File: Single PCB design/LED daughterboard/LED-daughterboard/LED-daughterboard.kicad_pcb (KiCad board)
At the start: 2 copper layers, 23.4 x 17 mm, 9 parts, among them J1 Conn_01x03_Male, J2 Conn_01x02_Male

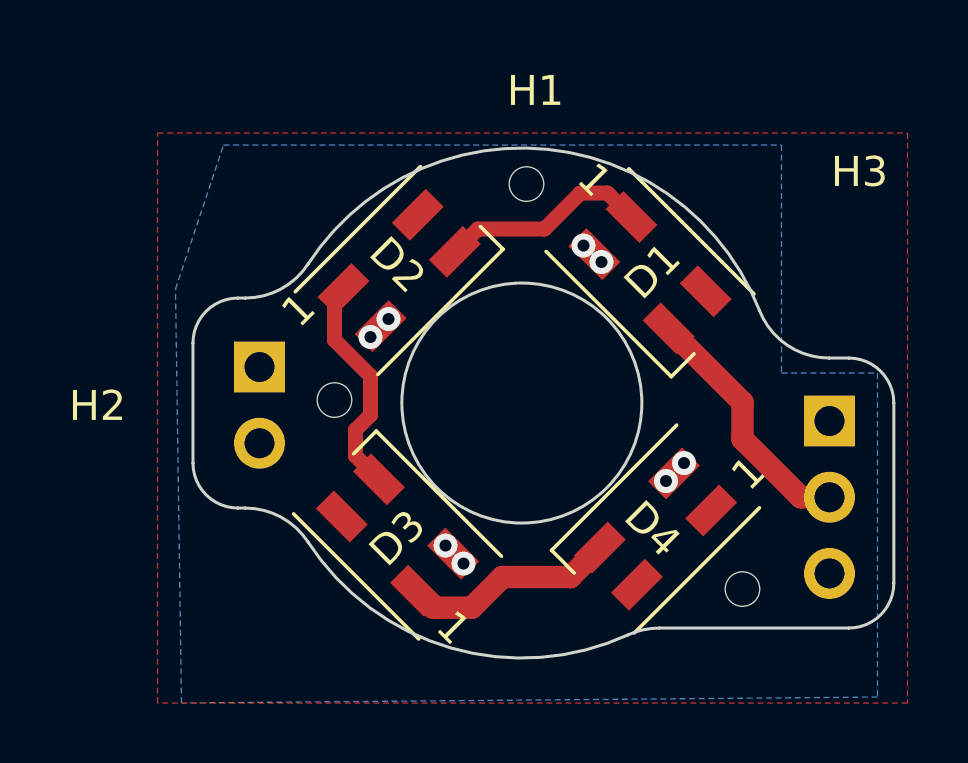
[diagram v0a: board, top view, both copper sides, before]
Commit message: Silkscreen changes
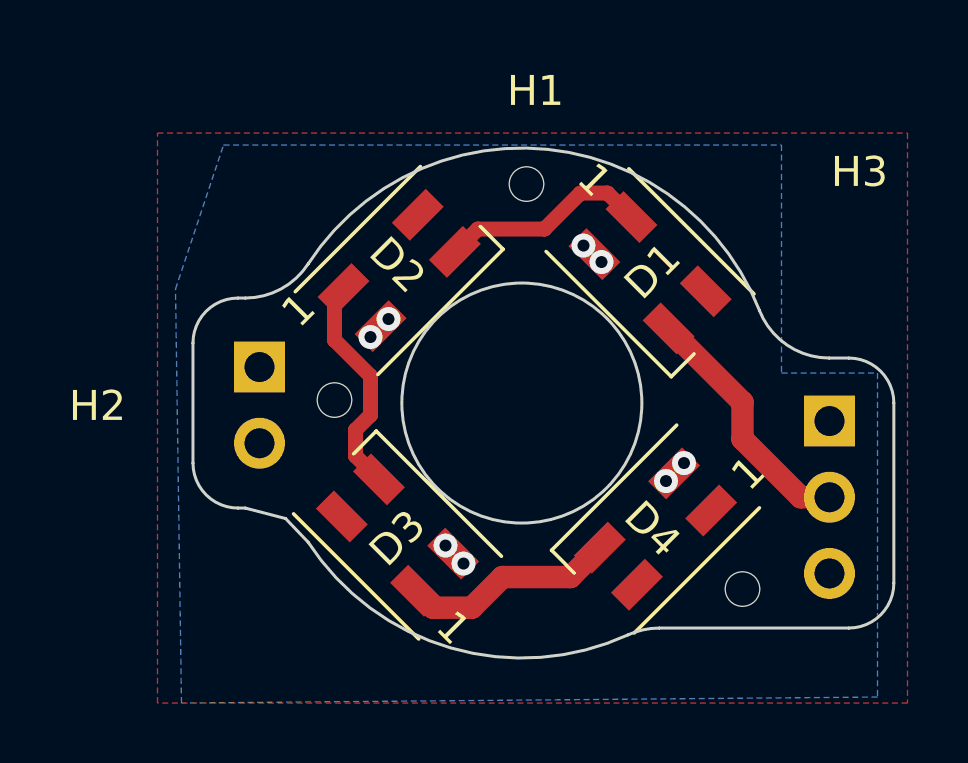
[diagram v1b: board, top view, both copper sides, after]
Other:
- outline, holes or cut-outs redrawn
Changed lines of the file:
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@@
   (general
     (thickness 1.6)
-    (drawings 17)
+    (drawings 18)
     (tracks 32)
     (modules 9)
@@
     )
   )
+  (gr_line (start -3.979118 -5.363636) (end -4.729925 -6.149999) (layer "Edge.Cuts") (width 0.1))
   (gr_arc (start -6.317425 -7.999999) (end -6.317425 -6.499999) (angle 90) (layer "Edge.Cuts") (width 0.1))
+  (gr_line (start 15.545075 -9.999999) (end 15.545075 -3.999999) (layer "Edge.Cuts") (width 0.1))
   (gr_arc (start 7.72765 0) (end 6.686156 -2.272727) (angle 24.61997733) (layer "Edge.Cuts") (width 0.1))
-  (gr_line (start 14.045075 -11.499999) (end 13.392025 -11.499999) (layer "Edge.Cuts") (width 0.1))
   (gr_arc (start -6.317425 -11.999999) (end -7.817425 -11.999999) (angle 90) (layer "Edge.Cuts") (width 0.1))
   (gr_line (start -7.817425 -11.999999) (end -7.817425 -7.999999) (layer "Edge.Cuts") (width 0.1))
@@
   (gr_arc (start 3.145075 -9.999999) (end -3.979119 -14.636363) (angle 125.6205826) (layer "Edge.Cuts") (width 0.1))
   (gr_arc (start 3.145075 -9.999999) (end 6.686156 -2.272727) (angle 81.56424618) (layer "Edge.Cuts") (width 0.1))
-  (gr_arc (start 13.392025 -13.999999) (end 13.392025 -11.499999) (angle 68.67631374) (layer "Edge.Cuts") (width 0.1))
+  (gr_arc (start 13.392026 -13.999999) (end 13.392026 -11.499999) (angle 68.67631374) (layer "Edge.Cuts") (width 0.1))
+  (gr_line (start -4.729925 -6.149999) (end -6.07447 -6.499999) (layer "Edge.Cuts") (width 0.1))
   (gr_circle (center 3.145075 -9.999999) (end -0.854925 -9.999999) (layer "Edge.Cuts") (width 0.1))
   (gr_line (start -6.317425 -6.499999) (end -6.07447 -6.499999) (layer "Edge.Cuts") (width 0.1))
-  (gr_line (start 7.72765 -2.499999) (end 14.045075 -2.499999) (layer "Edge.Cuts") (width 0.1))
-  (gr_arc (start -6.07447 -3.999999) (end -6.07447 -6.499999) (angle 56.94426885) (layer "Edge.Cuts") (width 0.1))
-  (gr_line (start 15.545075 -3.999999) (end 15.545075 -9.999999) (layer "Edge.Cuts") (width 0.1))
+  (gr_line (start 13.392026 -11.499999) (end 14.045075 -11.499999) (layer "Edge.Cuts") (width 0.1))
+  (gr_line (start 14.045075 -2.499999) (end 7.72765 -2.5) (layer "Edge.Cuts") (width 0.1))
   (segment (start 1.674874 -15.8) (end 3.9 -15.8) (width 0.5) (layer "F.Cu") (net 1))
   (segment (start 0.91231 -15.037436) (end 1.674874 -15.8) (width 0.5) (layer "F.Cu") (net 1))
